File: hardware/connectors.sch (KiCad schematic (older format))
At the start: 14 parts

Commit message: hardware: add terminal blocks
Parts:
- removed J? (x2): Conn_01x08, symbol Connector_Generic:Conn_01x08
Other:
- note removed: "Always on AUX connections"
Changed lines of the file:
@@
 $Descr A4 11693 8268
 encoding utf-8
-Sheet 3 3
+Sheet 3 4
 Title ""
 Date ""
@@
 	1    0    0    -1
 $EndComp
-$Comp
-L Connector_Generic:Conn_01x08 J?
-U 1 1 60A000AA
-P 9120 1760
-F 0 "J?" H 9200 1706 50  0000 L CNN
-F 1 "Conn_01x08" H 9200 1661 50  0001 L CNN
-F 2 "" H 9120 1760 50  0001 C CNN
-F 3 "~" H 9120 1760 50  0001 C CNN
-	1    9120 1760
-	1    0    0    -1
-$EndComp
-$Comp
-L power:GNDREF #PWR?
-U 1 1 60A03FCD
-P 8745 2330
-F 0 "#PWR?" H 8745 2080 50  0001 C CNN
-F 1 "GNDREF" H 8750 2157 50  0001 C CNN
-F 2 "" H 8745 2330 50  0001 C CNN
-F 3 "" H 8745 2330 50  0001 C CNN
-	1    8745 2330
-	1    0    0    -1
-$EndComp
-Wire Wire Line
-	8745 2330 8745 2160
-Wire Wire Line
-	8745 1560 8920 1560
-Wire Wire Line
-	8920 1760 8745 1760
-Connection ~ 8745 1760
-Wire Wire Line
-	8745 1760 8745 1560
-Wire Wire Line
-	8920 1960 8745 1960
-Connection ~ 8745 1960
-Wire Wire Line
-	8745 1960 8745 1760
-Wire Wire Line
-	8920 2160 8745 2160
-Connection ~ 8745 2160
-Wire Wire Line
-	8745 2160 8745 1960
-Wire Wire Line
-	8920 1460 8680 1460
-Wire Wire Line
-	8920 1660 8680 1660
-Wire Wire Line
-	8920 1860 8680 1860
-Wire Wire Line
-	8920 2060 8680 2060
-$Comp
-L Connector_Generic:Conn_01x08 J?
-U 1 1 60A65CC7
-P 9155 3335
-F 0 "J?" H 9235 3281 50  0000 L CNN
-F 1 "Conn_01x08" H 9235 3236 50  0001 L CNN
-F 2 "" H 9155 3335 50  0001 C CNN
-F 3 "~" H 9155 3335 50  0001 C CNN
-	1    9155 3335
-	1    0    0    -1
-$EndComp
-$Comp
-L power:GNDREF #PWR?
-U 1 1 60A65CCD
-P 8780 3905
-F 0 "#PWR?" H 8780 3655 50  0001 C CNN
-F 1 "GNDREF" H 8785 3732 50  0001 C CNN
-F 2 "" H 8780 3905 50  0001 C CNN
-F 3 "" H 8780 3905 50  0001 C CNN
-	1    8780 3905
-	1    0    0    -1
-$EndComp
-Wire Wire Line
-	8780 3905 8780 3735
-Wire Wire Line
-	8780 3135 8955 3135
-Wire Wire Line
-	8955 3335 8780 3335
-Connection ~ 8780 3335
-Wire Wire Line
-	8780 3335 8780 3135
-Wire Wire Line
-	8955 3535 8780 3535
-Connection ~ 8780 3535
-Wire Wire Line
-	8780 3535 8780 3335
-Wire Wire Line
-	8955 3735 8780 3735
-Connection ~ 8780 3735
-Wire Wire Line
-	8780 3735 8780 3535
-Wire Wire Line
-	8955 3035 8715 3035
-Wire Wire Line
-	8955 3235 8715 3235
-Wire Wire Line
-	8955 3435 8715 3435
-Wire Wire Line
-	8955 3635 8715 3635
-Text HLabel 8680 1460 0    50   Input ~ 0
-AUX_SW_1
-Text HLabel 8680 1660 0    50   Input ~ 0
-AUX_SW_2
-Text HLabel 8680 1860 0    50   Input ~ 0
-AUX_SW_3
-Text HLabel 8680 2060 0    50   Input ~ 0
-AUX_SW_4
-$Comp
-L power:+12V #PWR?
-U 1 1 60A7402C
-P 8715 2930
-F 0 "#PWR?" H 8715 2780 50  0001 C CNN
-F 1 "+12V" H 8730 3103 50  0000 C CNN
-F 2 "" H 8715 2930 50  0001 C CNN
-F 3 "" H 8715 2930 50  0001 C CNN
-	1    8715 2930
-	1    0    0    -1
-$EndComp
-Wire Wire Line
-	8715 2930 8715 3035
 Wire Bus Line
 	1645 1245 1645 2360
@@
 Wire Bus Line
 	5025 4735 5025 5850
-Connection ~ 8715 3035
-Wire Wire Line
-	8715 3035 8715 3235
-Connection ~ 8715 3235
-Wire Wire Line
-	8715 3235 8715 3435
-Connection ~ 8715 3435
-Wire Wire Line
-	8715 3435 8715 3635
-Text Notes 9085 2785 0    50   ~ 0
-Always on AUX connections
 $EndSCHEMATC

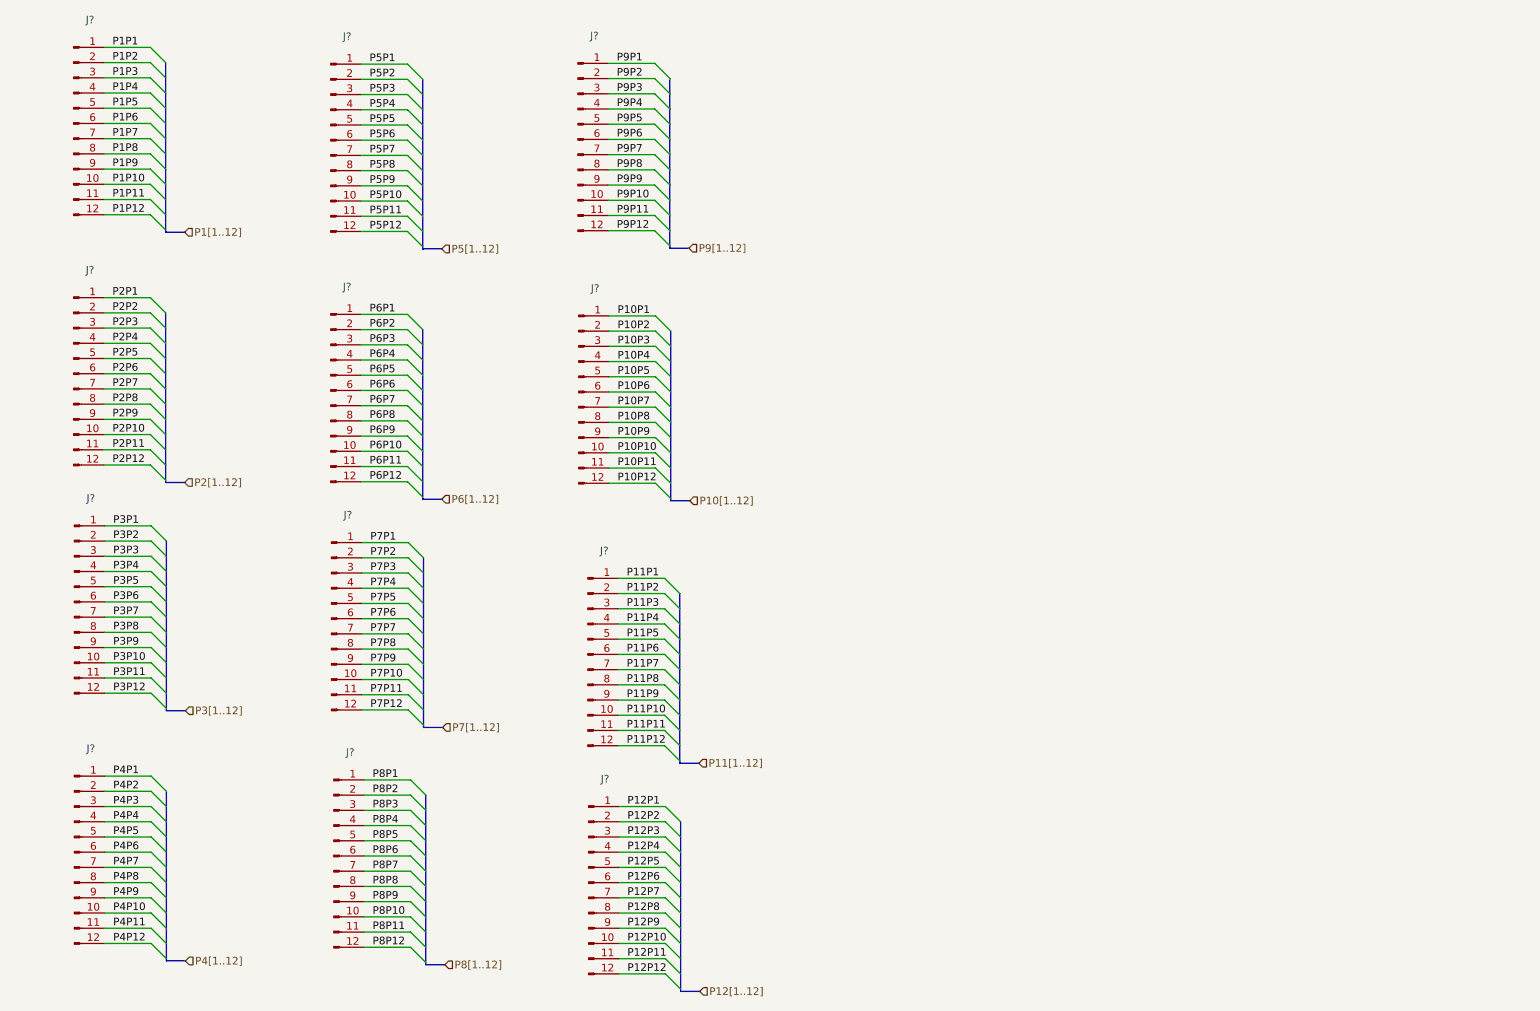
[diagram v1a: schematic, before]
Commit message: hardware: replace connectors connections with only ones which are relevant
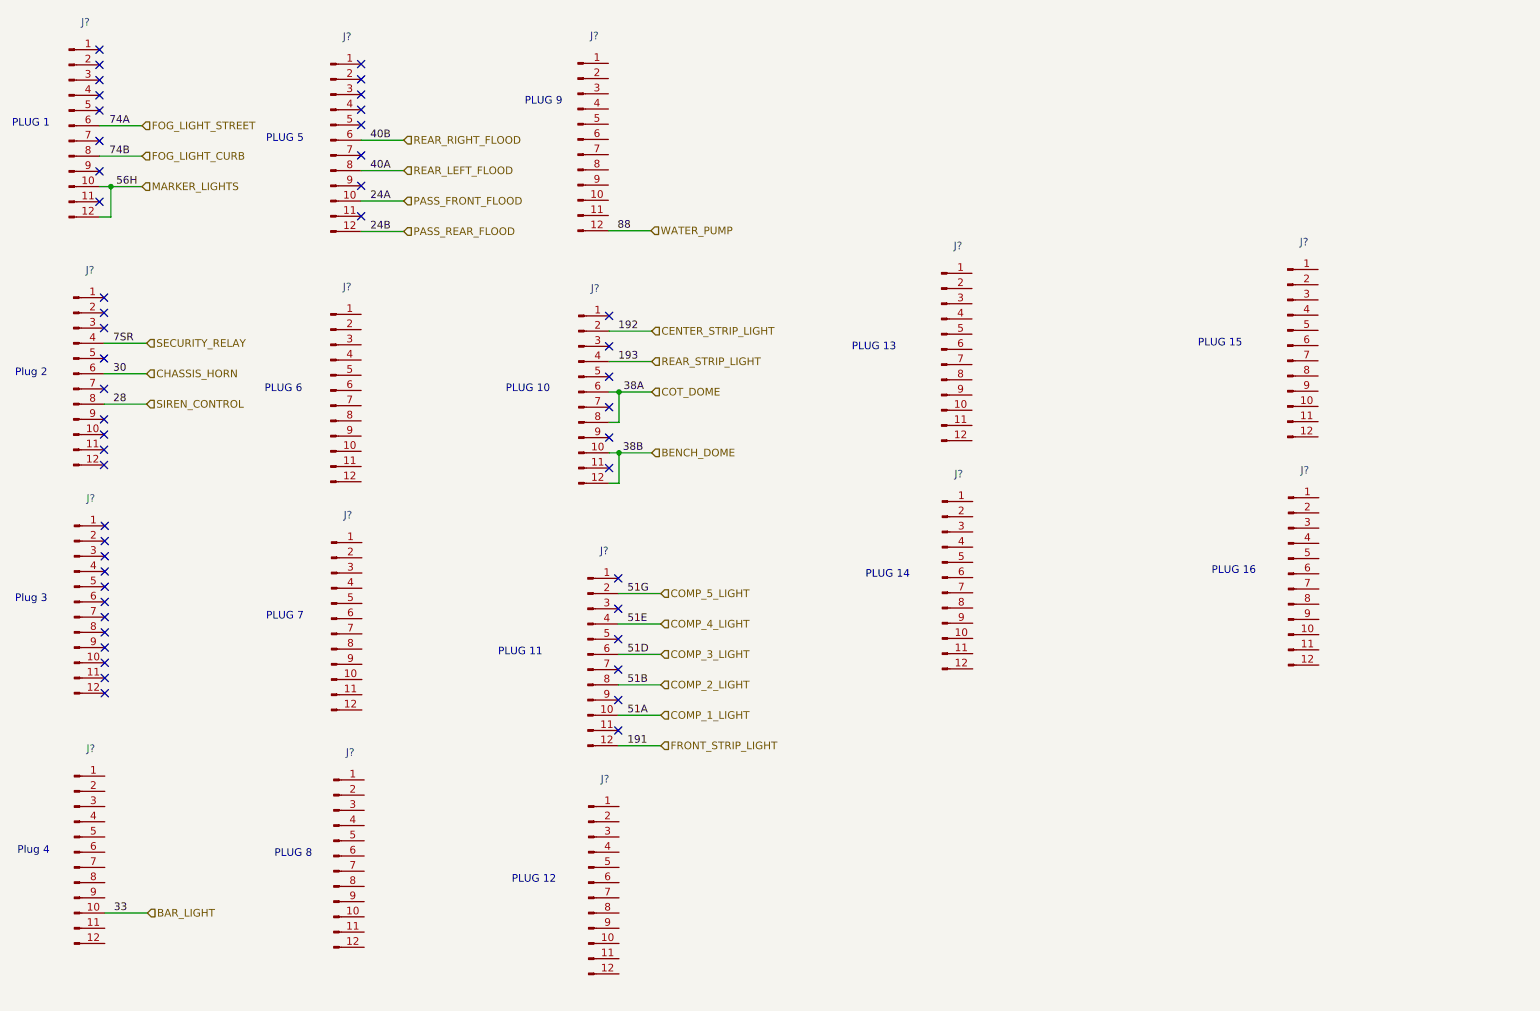
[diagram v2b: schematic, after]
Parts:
- removed J?: Conn_01x12_Male, Connector_Molex:Molex_KK-396_A-41791-0012_1x12_P3.96mm_Vertical, symbol Connector:Conn_01x12_Male
- added J? (x5): Conn_01x12_Male, Connector_Molex:Molex_KK-396_A-41791-0012_1x12_P3.96mm_Vertical, symbol Connector:Conn_01x12_Male
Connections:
- net P10P12 is gone; now on net BENCH_DOME: J?.12 (Pin_12)
- net P10P8 is gone; now on net COT_DOME: J?.8 (Pin_8)
- net P10P1: no longer names the net of J?.1 (Pin_1)
- net P10P10 renamed BENCH_DOME
- net P10P11: no longer names the net of J?.11 (Pin_11)
- net P10P2 renamed CENTER_STRIP_LIGHT
- net P10P3: no longer names the net of J?.3 (Pin_3)
- net P10P4 renamed REAR_STRIP_LIGHT
- net P10P5: no longer names the net of J?.5 (Pin_5)
- net P10P6 renamed COT_DOME
- net P10P7: no longer names the net of J?.7 (Pin_7)
- net P10P9: no longer names the net of J?.9 (Pin_9)
- net P11P1: no longer names the net of J?.1 (Pin_1)
- net P11P10 renamed COMP_1_LIGHT
- net P11P11: no longer names the net of J?.11 (Pin_11)
- net P11P12 renamed FRONT_STRIP_LIGHT
- net P11P2 renamed COMP_5_LIGHT
- net P11P3: no longer names the net of J?.3 (Pin_3)
- net P11P4 renamed COMP_4_LIGHT
- net P11P5: no longer names the net of J?.5 (Pin_5)
- net P11P6 renamed COMP_3_LIGHT
- net P11P7: no longer names the net of J?.7 (Pin_7)
- net P11P8 renamed COMP_2_LIGHT
- net P11P9: no longer names the net of J?.9 (Pin_9)
- net P12P1: no longer names the net of J?.1 (Pin_1)
- net P12P10: no longer names the net of J?.10 (Pin_10)
- net P12P11: no longer names the net of J?.11 (Pin_11)
- net P12P12: no longer names the net of J?.12 (Pin_12)
- net P12P2: no longer names the net of J?.2 (Pin_2)
- net P12P3: no longer names the net of J?.3 (Pin_3)
- net P12P4: no longer names the net of J?.4 (Pin_4)
- net P12P5: no longer names the net of J?.5 (Pin_5)
- net P12P6: no longer names the net of J?.6 (Pin_6)
- net P12P7: no longer names the net of J?.7 (Pin_7)
- net P12P8: no longer names the net of J?.8 (Pin_8)
- net P12P9: no longer names the net of J?.9 (Pin_9)
- net P2P1: no longer names the net of J?.1 (Pin_1)
- net P2P10: no longer names the net of J?.10 (Pin_10)
- net P2P11: no longer names the net of J?.11 (Pin_11)
- net P2P12: no longer names the net of J?.12 (Pin_12)
- net P2P2: no longer names the net of J?.2 (Pin_2)
- net P2P3: no longer names the net of J?.3 (Pin_3)
- net P2P4 renamed SECURITY_RELAY
- net P2P5: no longer names the net of J?.5 (Pin_5)
- net P2P6 renamed CHASSIS_HORN
- net P2P7: no longer names the net of J?.7 (Pin_7)
- net P2P8 renamed SIREN_CONTROL
- net P2P9: no longer names the net of J?.9 (Pin_9)
- net P3P1: no longer names the net of J?.1 (Pin_1)
- net P3P10: no longer names the net of J?.10 (Pin_10)
- net P3P11: no longer names the net of J?.11 (Pin_11)
- net P3P12: no longer names the net of J?.12 (Pin_12)
- net P3P2: no longer names the net of J?.2 (Pin_2)
- net P3P3: no longer names the net of J?.3 (Pin_3)
- net P3P4: no longer names the net of J?.4 (Pin_4)
- net P3P5: no longer names the net of J?.5 (Pin_5)
- net P3P6: no longer names the net of J?.6 (Pin_6)
- net P3P7: no longer names the net of J?.7 (Pin_7)
- net P3P8: no longer names the net of J?.8 (Pin_8)
- net P3P9: no longer names the net of J?.9 (Pin_9)
- net P4P1: no longer names the net of J?.1 (Pin_1)
- net P4P10 renamed BAR_LIGHT
- net P4P11: no longer names the net of J?.11 (Pin_11)
- net P4P12: no longer names the net of J?.12 (Pin_12)
- net P4P2: no longer names the net of J?.2 (Pin_2)
- net P4P3: no longer names the net of J?.3 (Pin_3)
- net P4P4: no longer names the net of J?.4 (Pin_4)
- net P4P5: no longer names the net of J?.5 (Pin_5)
- net P4P6: no longer names the net of J?.6 (Pin_6)
- net P4P7: no longer names the net of J?.7 (Pin_7)
- net P4P8: no longer names the net of J?.8 (Pin_8)
- net P4P9: no longer names the net of J?.9 (Pin_9)
- net P5P1: no longer names the net of J?.1 (Pin_1)
- net P5P10 renamed PASS_FRONT_FLOOD
- net P5P11: no longer names the net of J?.11 (Pin_11)
- net P5P12 renamed PASS_REAR_FLOOD
- net P5P2: no longer names the net of J?.2 (Pin_2)
- net P5P3: no longer names the net of J?.3 (Pin_3)
- net P5P4: no longer names the net of J?.4 (Pin_4)
- net P5P5: no longer names the net of J?.5 (Pin_5)
- net P5P6 renamed REAR_RIGHT_FLOOD
- net P5P7: no longer names the net of J?.7 (Pin_7)
- net P5P8 renamed REAR_LEFT_FLOOD
- net P5P9: no longer names the net of J?.9 (Pin_9)
- net P6P1: no longer names the net of J?.1 (Pin_1)
- net P6P10: no longer names the net of J?.10 (Pin_10)
- net P6P11: no longer names the net of J?.11 (Pin_11)
- net P6P12: no longer names the net of J?.12 (Pin_12)
- net P6P2: no longer names the net of J?.2 (Pin_2)
- net P6P3: no longer names the net of J?.3 (Pin_3)
- net P6P4: no longer names the net of J?.4 (Pin_4)
- net P6P5: no longer names the net of J?.5 (Pin_5)
- net P6P6: no longer names the net of J?.6 (Pin_6)
- net P6P7: no longer names the net of J?.7 (Pin_7)
- net P6P8: no longer names the net of J?.8 (Pin_8)
- net P6P9: no longer names the net of J?.9 (Pin_9)
- net P7P1: no longer names the net of J?.1 (Pin_1)
- net P7P10: no longer names the net of J?.10 (Pin_10)
- net P7P11: no longer names the net of J?.11 (Pin_11)
- net P7P12: no longer names the net of J?.12 (Pin_12)
- net P7P2: no longer names the net of J?.2 (Pin_2)
- net P7P3: no longer names the net of J?.3 (Pin_3)
- net P7P4: no longer names the net of J?.4 (Pin_4)
- net P7P5: no longer names the net of J?.5 (Pin_5)
- net P7P6: no longer names the net of J?.6 (Pin_6)
- net P7P7: no longer names the net of J?.7 (Pin_7)
- net P7P8: no longer names the net of J?.8 (Pin_8)
- net P7P9: no longer names the net of J?.9 (Pin_9)
- net P8P1: no longer names the net of J?.1 (Pin_1)
- net P8P10: no longer names the net of J?.10 (Pin_10)
- net P8P11: no longer names the net of J?.11 (Pin_11)
- net P8P12: no longer names the net of J?.12 (Pin_12)
- net P8P2: no longer names the net of J?.2 (Pin_2)
- net P8P3: no longer names the net of J?.3 (Pin_3)
- net P8P4: no longer names the net of J?.4 (Pin_4)
- net P8P5: no longer names the net of J?.5 (Pin_5)
- net P8P6: no longer names the net of J?.6 (Pin_6)
- net P8P7: no longer names the net of J?.7 (Pin_7)
- net P8P8: no longer names the net of J?.8 (Pin_8)
- net P8P9: no longer names the net of J?.9 (Pin_9)
- net P9P1: no longer names the net of J?.1 (Pin_1)
- net P9P10: no longer names the net of J?.10 (Pin_10)
- net P9P11: no longer names the net of J?.11 (Pin_11)
- net P9P12 renamed WATER_PUMP
- net P9P2: no longer names the net of J?.2 (Pin_2)
- net P9P3: no longer names the net of J?.3 (Pin_3)
- net P9P4: no longer names the net of J?.4 (Pin_4)
- net P9P5: no longer names the net of J?.5 (Pin_5)
- net P9P6: no longer names the net of J?.6 (Pin_6)
- net P9P7: no longer names the net of J?.7 (Pin_7)
- net P9P8: no longer names the net of J?.8 (Pin_8)
- net P9P9: no longer names the net of J?.9 (Pin_9)
- new net FOG_LIGHT_CURB: J?.8 (Pin_8)
- new net FOG_LIGHT_STREET: J?.6 (Pin_6)
- new net MARKER_LIGHTS: J?.10 (Pin_10), J?.12 (Pin_12)
- no-connect marks 0 -> 49
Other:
- note added: "PLUG 1"
- note added: "PLUG 10"
- note added: "PLUG 11"
- note added: "PLUG 12"
- note added: "PLUG 13"
- note added: "PLUG 14"
- note added: "PLUG 15"
- note added: "PLUG 16"
- note added: "PLUG 5"
- note added: "PLUG 6"
- note added: "PLUG 7"
- note added: "PLUG 8"
- note added: "PLUG 9"
- note added: "Plug 2"
- note added: "Plug 3"
- note added: "Plug 4"

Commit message: hardware: label unused plug pins
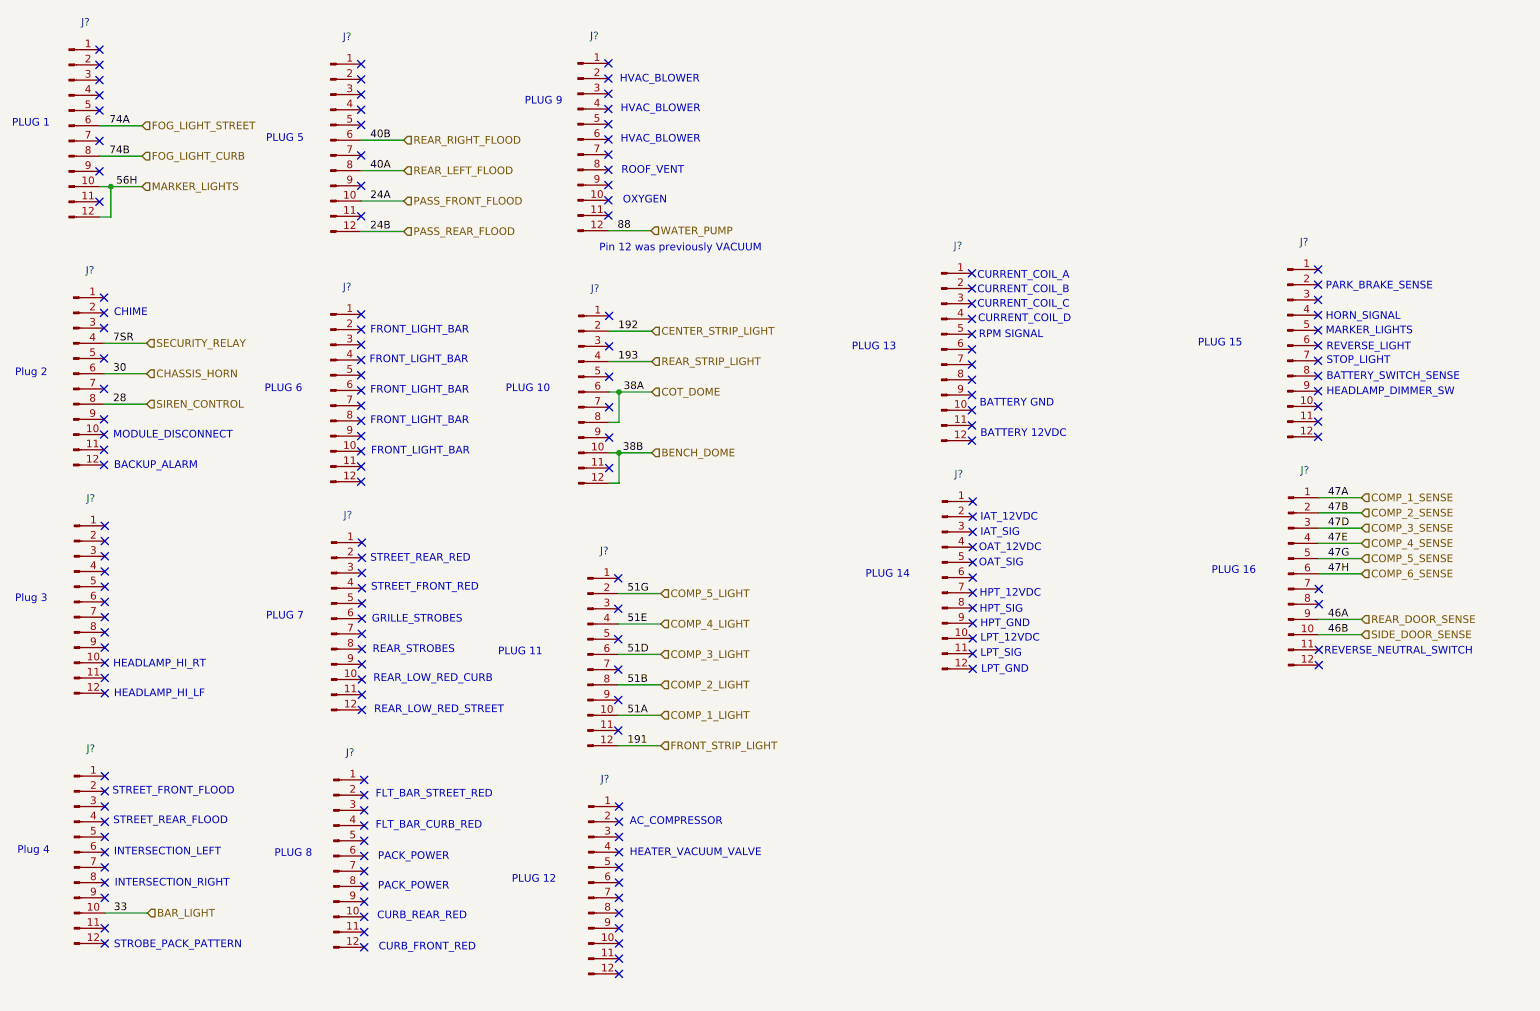
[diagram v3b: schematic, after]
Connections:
- net COMP_1_SENSE: now reaches J?.1 (Pin_1)
- net SIDE_DOOR_SENSE: now reaches J?.10 (Pin_10)
- net COMP_2_SENSE: now reaches J?.2 (Pin_2)
- net COMP_3_SENSE: now reaches J?.3 (Pin_3)
- net COMP_4_SENSE: now reaches J?.4 (Pin_4)
- net COMP_5_SENSE: now reaches J?.5 (Pin_5)
- net COMP_6_SENSE: now reaches J?.6 (Pin_6)
- net REAR_DOOR_SENSE: now reaches J?.9 (Pin_9)
- no-connect marks 49 -> 159
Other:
- note added: "AC_COMPRESSOR"
- note added: "BACKUP_ALARM"
- note added: "BATTERY 12VDC"
- note added: "BATTERY GND"
- note added: "BATTERY_SWITCH_SENSE"
- note added: "CHIME"
- note added: "CURB_FRONT_RED"
- note added: "CURB_REAR_RED"
- note added: "CURRENT_COIL_A"
- note added: "CURRENT_COIL_B"
- note added: "CURRENT_COIL_C"
- note added: "CURRENT_COIL_D"
- note added: "FLT_BAR_CURB_RED"
- note added: "FLT_BAR_STREET_RED"
- note added: "FRONT_LIGHT_BAR"
- note added: "GRILLE_STROBES"
- note added: "HEADLAMP_DIMMER_SW"
- note added: "HEADLAMP_HI_LF"
- note added: "HEADLAMP_HI_RT"
- note added: "HEATER_VACUUM_VALVE"
- note added: "HORN_SIGNAL"
- note added: "HPT_12VDC"
- note added: "HPT_GND"
- note added: "HPT_SIG"
- note added: "HVAC_BLOWER"
- note added: "IAT_12VDC"
- note added: "IAT_SIG"
- note added: "INTERSECTION_LEFT"
- note added: "INTERSECTION_RIGHT"
- note added: "LPT_12VDC"
- note added: "LPT_GND"
- note added: "LPT_SIG"
- note added: "MARKER_LIGHTS"
- note added: "MODULE_DISCONNECT"
- note added: "OAT_12VDC"
- note added: "OAT_SIG"
- note added: "OXYGEN"
- note added: "PACK_POWER"
- note added: "PARK_BRAKE_SENSE"
- note added: "Pin 12 was previously VACUUM"
- note added: "REAR_LOW_RED_CURB"
- note added: "REAR_LOW_RED_STREET"
- note added: "REAR_STROBES"
- note added: "REVERSE_LIGHT"
- note added: "REVERSE_NEUTRAL_SWITCH"
- note added: "ROOF_VENT"
- note added: "RPM SIGNAL"
- note added: "STOP_LIGHT"
- note added: "STREET_FRONT_FLOOD"
- note added: "STREET_FRONT_RED"
- note added: "STREET_REAR_FLOOD"
- note added: "STREET_REAR_RED"
- note added: "STROBE_PACK_PATTERN"
